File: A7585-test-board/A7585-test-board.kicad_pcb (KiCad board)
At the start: 4 copper layers, 91.4 x 105.4 mm, 32 parts, among them J1 Conn_01x04_Female, J100 Conn_Coaxial_Power, J2 Conn_01x20, J3 Conn_01x20, J4 Conn_Coaxial_Power, SW201 SW_SPDT, SW302 SW_Push_SPDT, SW303 SW_Push_SPDT, U100 MPM3610, U200 A7585D, U300 Pico

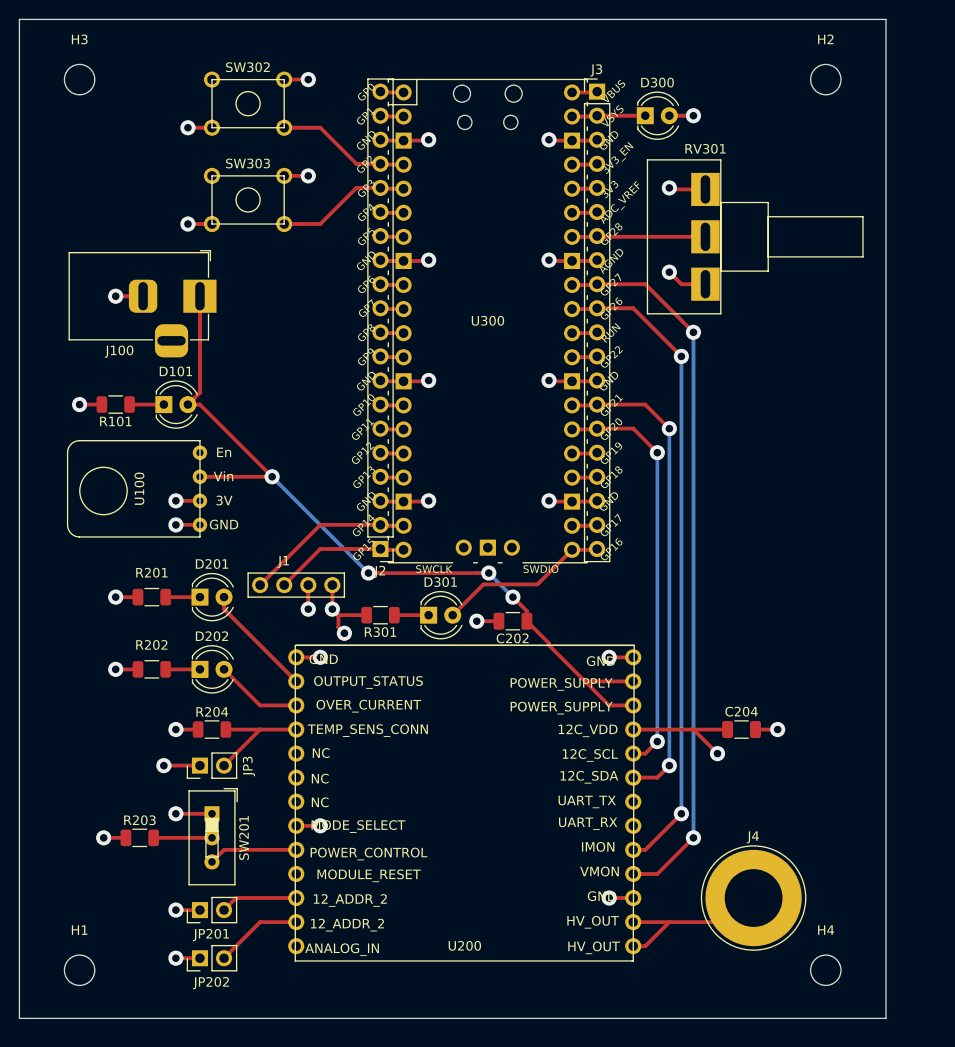
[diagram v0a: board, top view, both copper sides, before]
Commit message: Fixed power planes
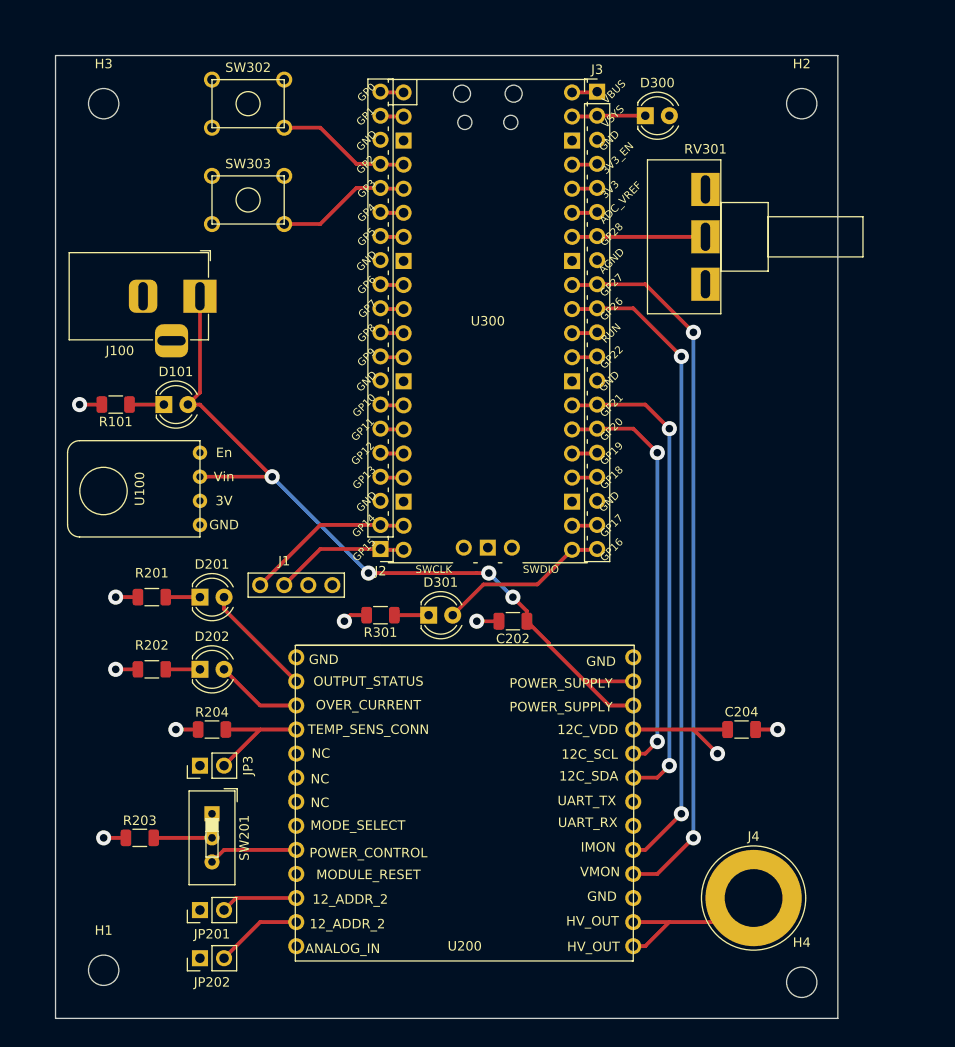
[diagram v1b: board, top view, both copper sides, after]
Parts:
- moved H2 3.59 mm to (142.2, 61.0)
- moved H3 3.59 mm to (68.6, 61.0)
- moved H4 2.84 mm to (142.2, 153.7)
- moved H1 2.54 mm to (68.6, 152.4)
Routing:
- net GND: track 98.8 -> 15.3 mm, vias 28 -> 6
- net VCC: track 35.3 -> 18.2 mm, vias 9 -> 3
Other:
- board size 91.4 x 105.4 mm -> 82.6 x 101.6 mm

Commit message: Grounded mounting holes. Fixed power plane
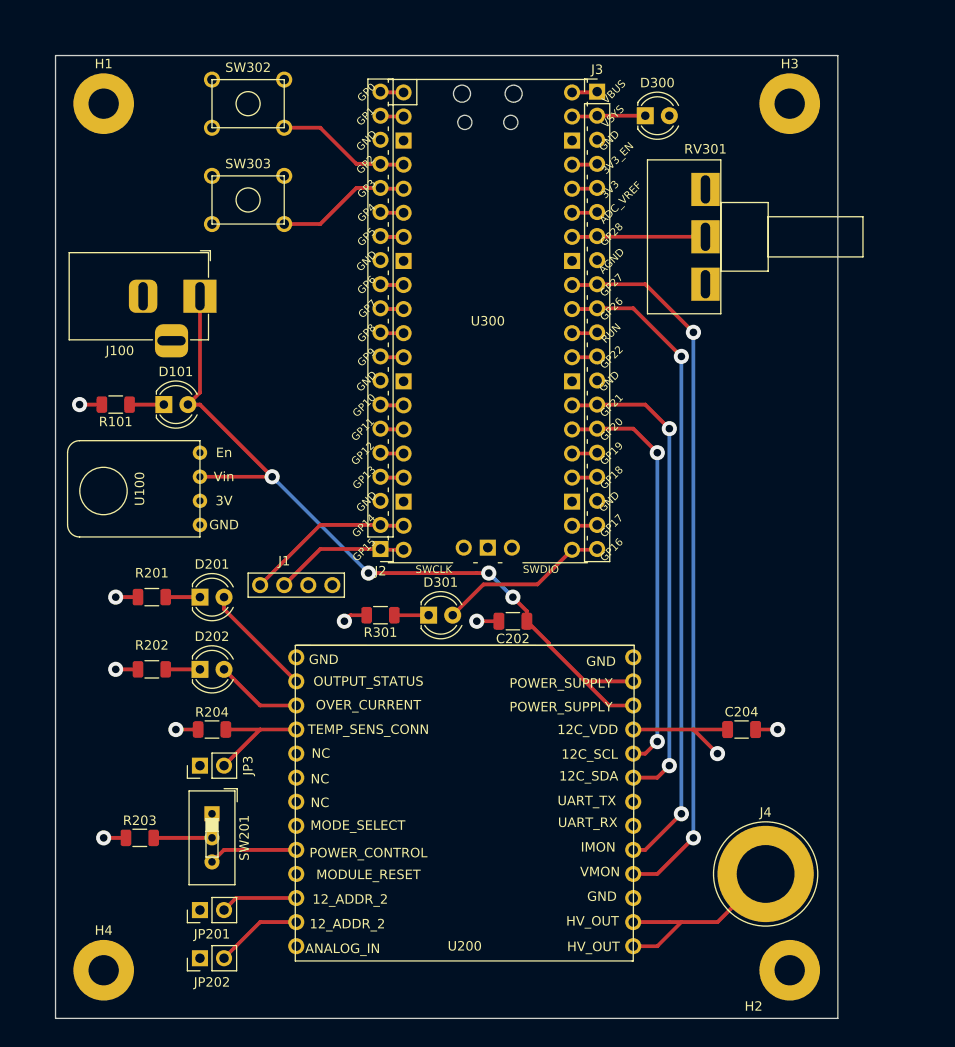
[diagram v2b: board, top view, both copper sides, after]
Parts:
- H1, H2, H3, H4: value MountingHole -> MountingHole_Pad; footprint MountingHole:MountingHole_3.2mm_M3 -> MountingHole:MountingHole_3.2mm_M3_Pad
- moved H2 91.4 mm to (141.0, 152.4)
- moved H1 91.4 mm to (68.6, 61.0)
- moved H4 73.7 mm to (68.6, 152.4)
- moved H3 72.4 mm to (141.0, 61.0)
- moved J4 2.84 mm to (138.4, 142.2)
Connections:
- H1 pad 1: (no net) -> GND
- H2 pad 1: (no net) -> GND
- H3 pad 1: (no net) -> GND
- H4 pad 1: (no net) -> GND
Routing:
- net Net-(J4-Pad1): track 18.6 -> 22.2 mm

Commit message: New Banana Jacks
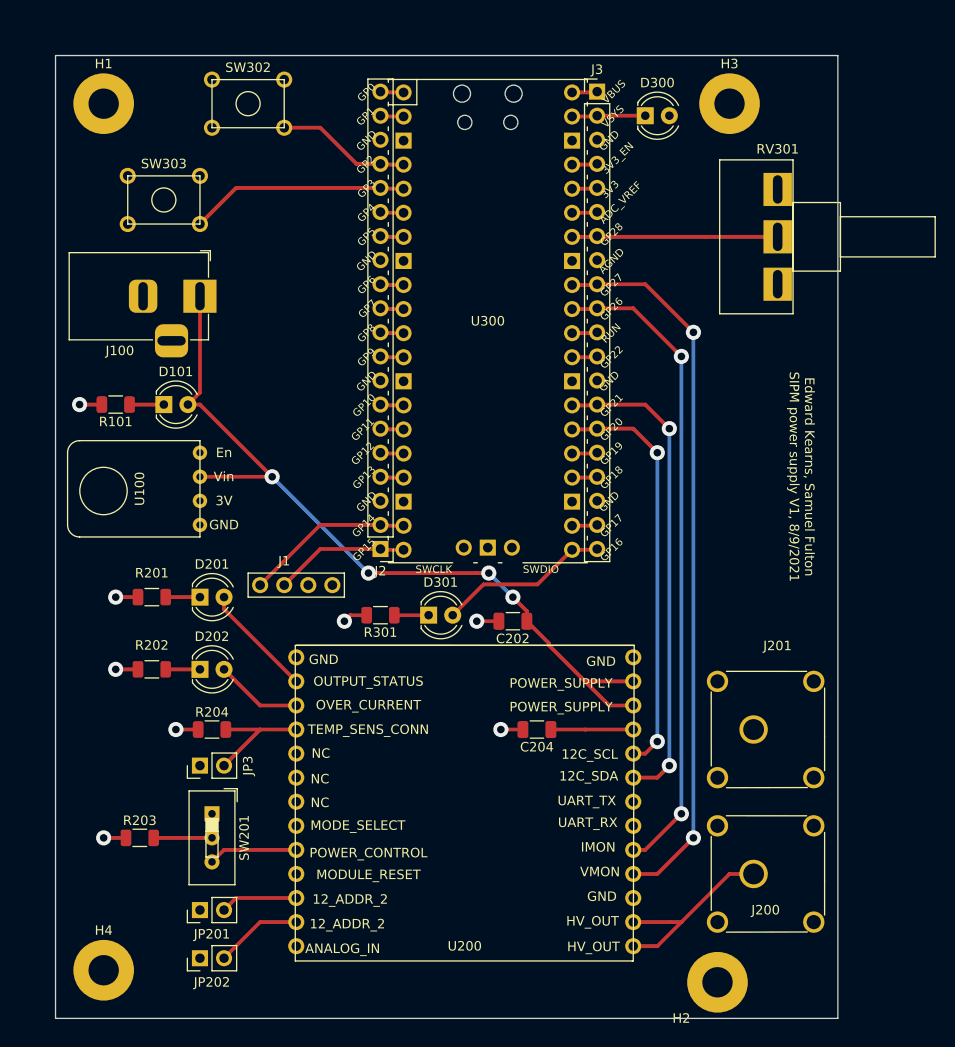
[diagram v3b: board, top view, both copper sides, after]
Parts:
- removed J4: Conn_Coaxial_Power, Connector:Banana_Jack_1Pin
- added J200: Conn_01x01_Female, A7585-test-board:SMA_Molex_73251-2200_Horizontal, F.Cu at (138.4, 142.2)
- added J201: Conn_01x01_Female, A7585-test-board:SMA_Molex_73251-2200_Horizontal, F.Cu at (138.4, 127.0)
- moved C204 21.6 mm to (114.3, 127.0), turned to 180 degrees
- moved SW303 8.89 mm to (73.7, 71.1)
- moved H2 7.73 mm to (133.3, 153.7)
- moved RV301 7.62 mm to (139.7, 80.0)
- moved H3 6.35 mm to (134.6, 61.0)
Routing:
- net Net-(J2-Pad16): track 14.2 -> 23.1 mm
- net Net-(J3-Pad7): track 14.3 -> 21.8 mm
- net VCC: track 18.2 -> 13.4 mm, vias 3 -> 2
- net Net-(J200-Pad1): track 22.2 -> 20.9 mm
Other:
- board text added: "Edward Kearns, Samuel Fulton SIPM power supply V1, 8/9/2021"
- board text removed: "Display"

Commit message: Add files via upload
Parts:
- added C205: 2.2 uF, Capacitor_SMD:C_1206_3216Metric, F.Cu at (127.0, 153.7)
- added C302: 2.2 uF, Capacitor_SMD:C_1206_3216Metric, F.Cu at (130.8, 67.3)
- added R302: 200, Resistor_SMD:R_1206_3216Metric, F.Cu at (127.0, 73.7)
- added SW301: Rotary Encoder PCB, Connector_PinHeader_2.54mm:PinHeader_1x05_P2.54mm_Vertical, F.Cu at (66.0, 72.4)
- added U301: LM4040LP-3, Package_TO_SOT_THT:TO-92_Inline, F.Cu at (132.1, 71.1)
- J200, J201: footprint A7585-test-board:SMA_Molex_73251-2200_Horizontal -> A7585-test-board:Bannana_Jack_2pin
- moved RV301 12.0 mm to (135.9, 91.4)
- moved J201 10.2 mm to (137.2, 137.2), turned to 0 degrees
- moved J200 4.02 mm to (137.2, 146.1), turned to 0 degrees
- moved H1 3.81 mm to (72.4, 61.0)
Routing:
- net Net-(J2-Pad12): track 2.47 -> 41.6 mm, vias 0 -> 2
- net Net-(J2-Pad11): track 2.47 -> 41.6 mm, vias 0 -> 2
- net Net-(C302-Pad1): track 2.68 -> 20.1 mm
- net GND: track 15.3 -> 32.7 mm, vias 6 -> 7
- net Net-(C205-Pad1): track 20.9 -> 12.6 mm
- net VCC: track 13.4 -> 15.7 mm, vias 2 -> 3
- net Net-(J3-Pad7): track 21.8 -> 22.8 mm
